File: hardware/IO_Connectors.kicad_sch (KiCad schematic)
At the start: 31 parts, among them J29 RJ12_Shielded, J3 USB_B_Micro, U8 TJA1040

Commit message: Intermediate checkin
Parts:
- removed EXP1, EXP2, EXP3: IDC 2x5, Connector_IDC:IDC-Header_2x05_P2.54mm_Vertical, symbol Connector_Generic:Conn_02x05_Odd_Even
- removed JP1: Jumper_2_Open, Connector_PinHeader_2.54mm:PinHeader_1x02_P2.54mm_Vertical, symbol Jumper:Jumper_2_Open
- removed R78: 10k, PrntrBoardV2:R_0603_1608Metric, symbol Device:R
- removed RN1, RN2: 4x470, Resistor_SMD:R_Array_Convex_4x0603, symbol Device:R_Pack04
- added R1, R45, R8: 10k, Resistor_SMD:R_0402_1005Metric, symbol Device:R
- C18: value 0.1uF -> 100nf; footprint PrntrBoardV2:C_0603_1608Metric -> Capacitor_SMD:C_0402_1005Metric; LCSC Part # C14663 -> C1525; Part # CC0603KRX7R9BB104 -> CL05B104KO5NNNC
- C19, C54: footprint PrntrBoardV2:C_0603_1608Metric -> Capacitor_SMD:C_0402_1005Metric; LCSC Part # C14663 -> C1525; Part # CC0603KRX7R9BB104 -> CL05B104KO5NNNC
- C55: footprint PrntrBoardV2:C_0603_1608Metric -> Capacitor_SMD:C_0402_1005Metric; LCSC Part # C14663 -> C1525; Part # CC0603KRX7R9BB104 -> CL05B104KO5NNNC; now in the parts list
- J29: footprint Connector_RJ:RJ12_Amphenol_54601 -> PrntrBoardV2:Wurth_615006143421
- R10, R11, R72: footprint PrntrBoardV2:R_0603_1608Metric -> Resistor_SMD:R_0402_1005Metric; LCSC Part # C23345 -> C25092; Part # 0603WAF220JT5E -> 0402WGF220JTCE
- R12: footprint PrntrBoardV2:R_0603_1608Metric -> Resistor_SMD:R_0402_1005Metric; LCSC Part # C25803 -> C25741; Part # 0603WAF1003T5E -> 0402WGF1003TCE
- R2, R73, R77: footprint PrntrBoardV2:R_0603_1608Metric -> Resistor_SMD:R_0402_1005Metric; LCSC Part # C25804 -> C25744; Part # 0603WAF1002T5E -> 0402WGF1002TCE
- R74, R75: footprint PrntrBoardV2:R_0603_1608Metric -> Resistor_SMD:R_0603_1608Metric
- R76: footprint PrntrBoardV2:R_0603_1608Metric -> Resistor_SMD:R_0402_1005Metric; LCSC Part # C25803 -> C25741; Part # 0603WAF1003T5E -> 0402WGF1003TCE; now in the parts list
- R9: footprint PrntrBoardV2:R_0603_1608Metric -> Resistor_SMD:R_0402_1005Metric; LCSC Part # C22843 -> C25867; Part # 0603WAF1501T5E -> 0402WGF1501TCE
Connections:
- net 3.3V: now also R1.1, R45.1, R8.2
- net SDIO_D2: now reaches XS1.1 (DAT2)
- net SDIO_D2: now also RN3.8 (R1.2)
- net SDIO_D1: now reaches XS1.8 (DAT1)
- net SDIO_D1: now also R45.2
- net at R2.2, XS1.9 (CD): now also R1.2; no longer RN3.5 (R4.2)
- net SPI1_MISO renamed SDIO_CMD
- net SDIO_CMD: now also XS1.3 (DI/CMD); no longer XS1.7 (DO/DAT0)
- removed net SPI1_MOSI: RN3.8 (R1.2), XS1.3 (DI/CMD)
- net SPI1_SCK renamed SDIO_CK
- net SDIO_CK: now also RN3.5 (R4.2); no longer RN3.7 (R2.2)
- net UART_RX renamed UART1_RX
- net UART_TX renamed UART1_TX
- net ~SD_CS renamed SDIO_D3
- net SDIO_D3: now also RN3.7 (R2.2)
- new net SDIO_D0: R8.1, XS1.7 (DO/DAT0)
- no-connect marks 7 -> 5
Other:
- note removed: "Optional if RJ12 connector is shielded."
- moved on the sheet: C18, C19, C54, C55, D1, F1, J29, J3, JP9, J_SER1, R10, R11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

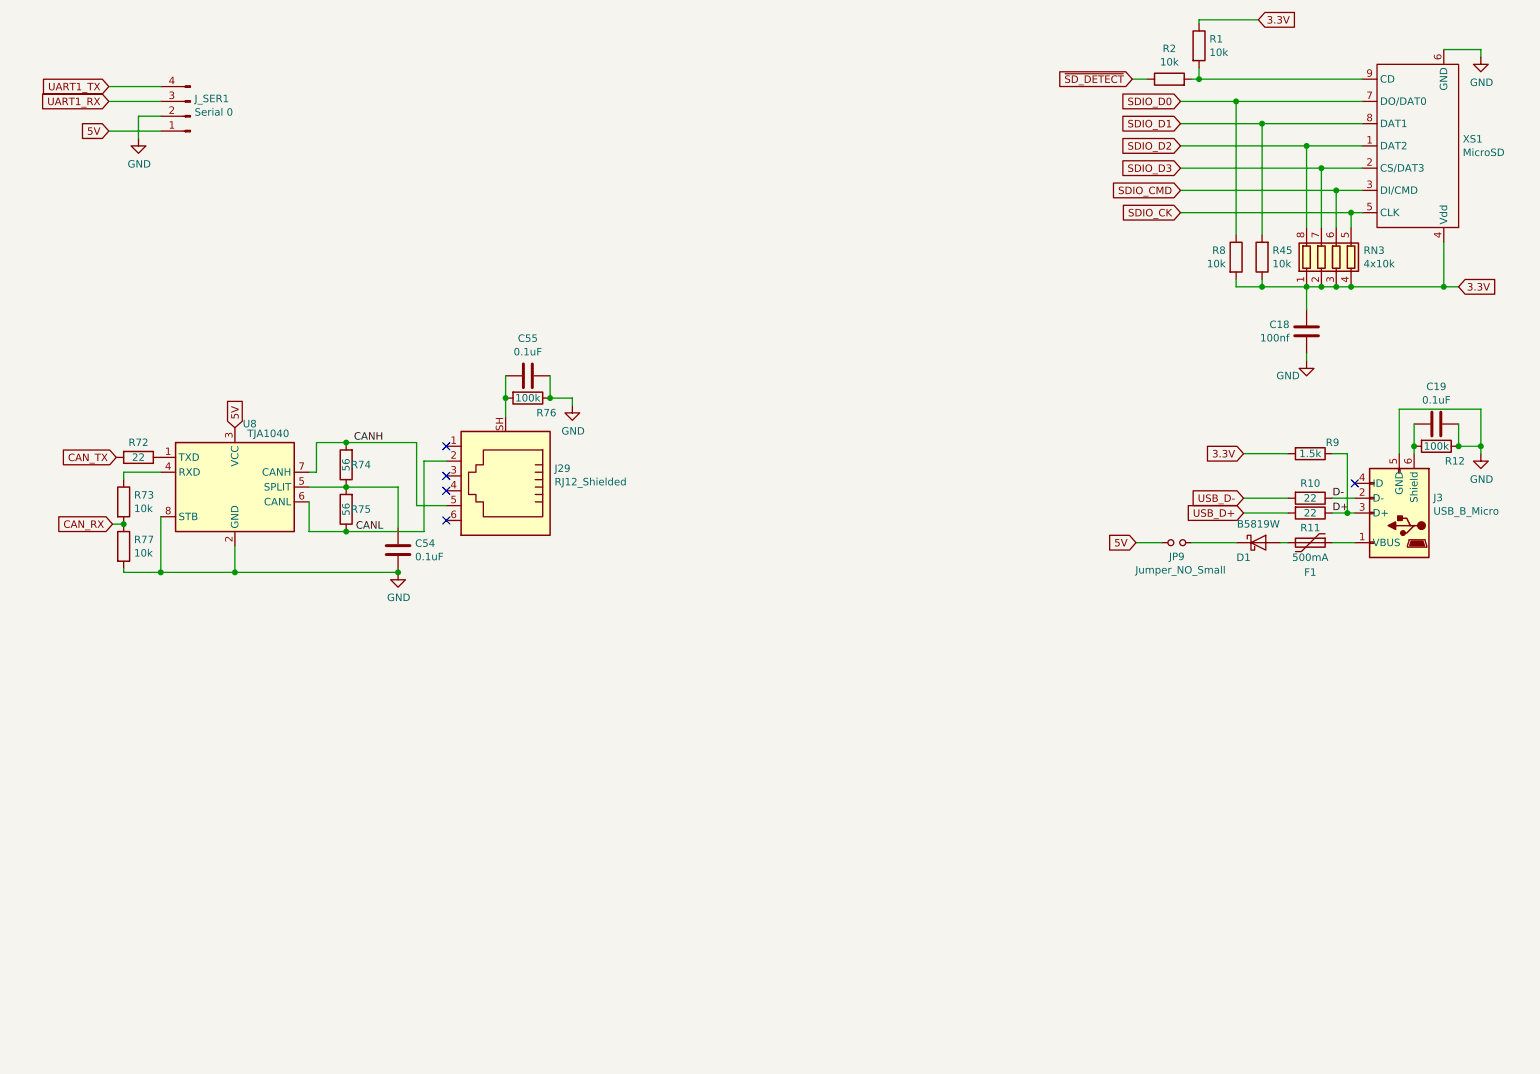
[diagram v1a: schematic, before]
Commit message: Add Wifi connector
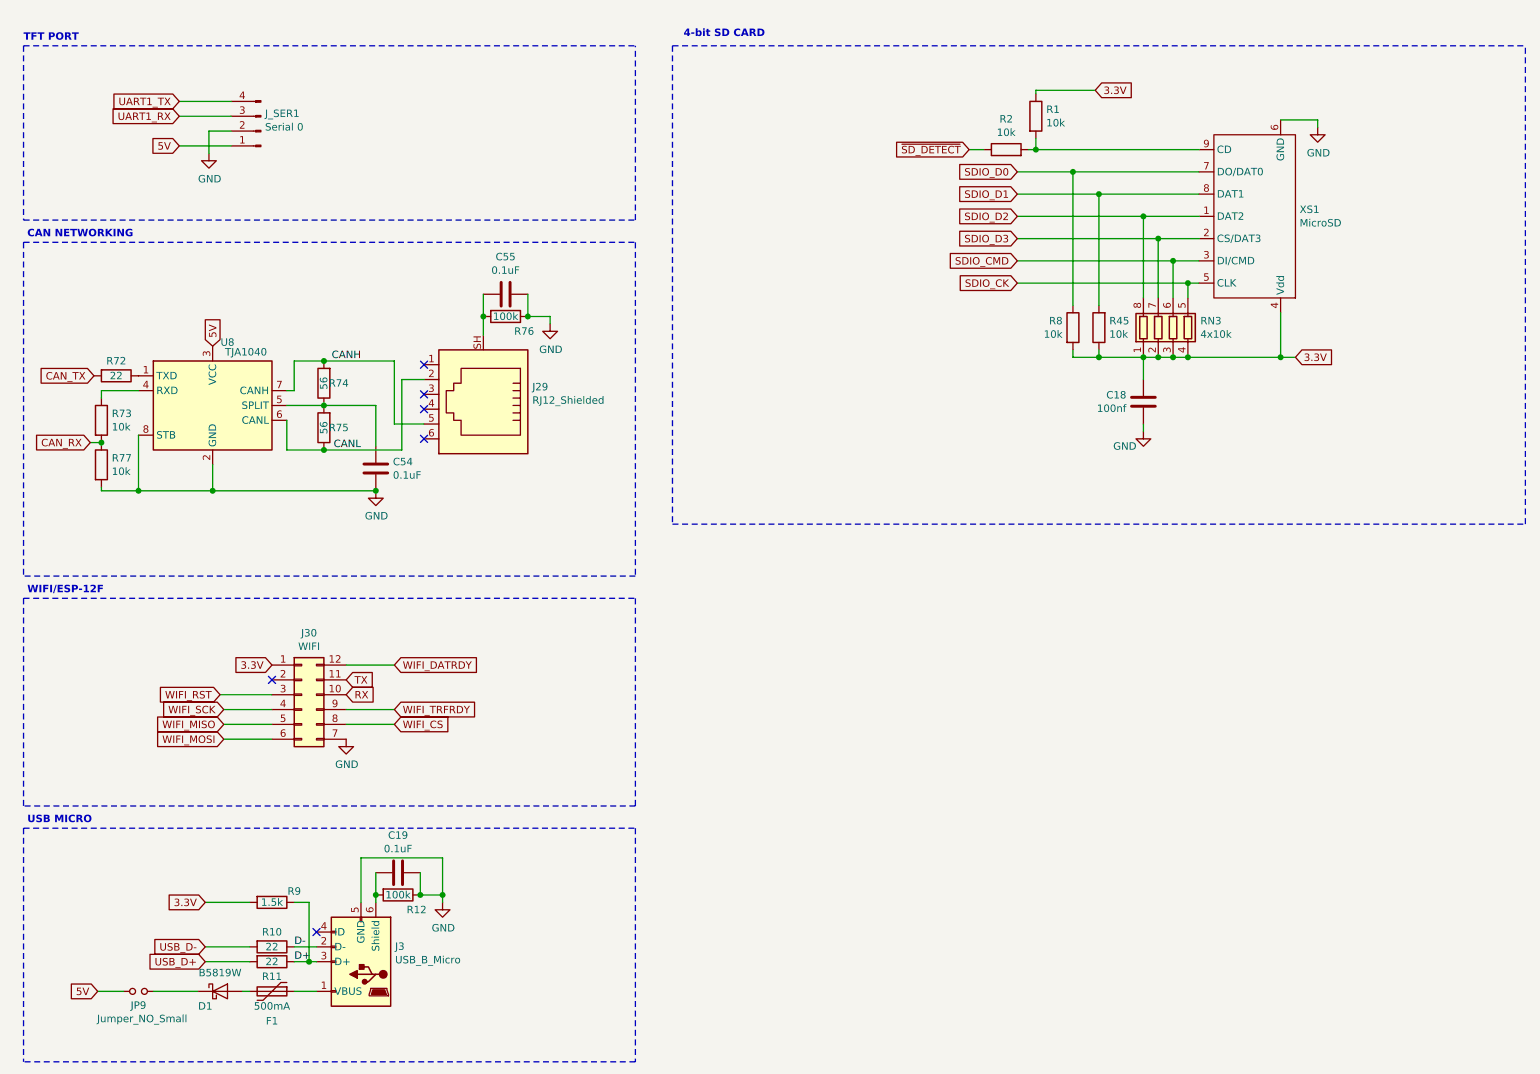
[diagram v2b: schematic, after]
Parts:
- added J30: WIFI, Connector_PinHeader_2.54mm:PinHeader_2x06_P2.54mm_Vertical, symbol Connector_Generic:Conn_02x06_Counter_Clockwise
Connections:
- net 3.3V: now also J30.1 (Pin_1)
- net GND: now also J30.7 (Pin_7)
- new net RX: J30.10 (Pin_10)
- new net TX: J30.11 (Pin_11)
- new net WIFI_CS: J30.8 (Pin_8)
- new net WIFI_DATRDY: J30.12 (Pin_12)
- new net WIFI_MISO: J30.5 (Pin_5)
- new net WIFI_MOSI: J30.6 (Pin_6)
- new net WIFI_RST: J30.3 (Pin_3)
- new net WIFI_SCK: J30.4 (Pin_4)
- new net WIFI_TRFRDY: J30.9 (Pin_9)
- no-connect marks 5 -> 6
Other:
- note added: "4-bit SD CARD"
- note added: "CAN NETWORKING"
- note added: "TFT PORT"
- note added: "USB MICRO"
- note added: "WIFI/ESP-12F"
- moved on the sheet: C18, C19, C54, C55, D1, F1, J29, J3, JP9, J_SER1, R1, R10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
